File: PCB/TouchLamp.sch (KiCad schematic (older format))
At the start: 14 parts, among them IC1 ATTINY2313-P, P1 PWR_LED_ISP, P3 Sensor, Q1 BC817-40, U1 LM78L05

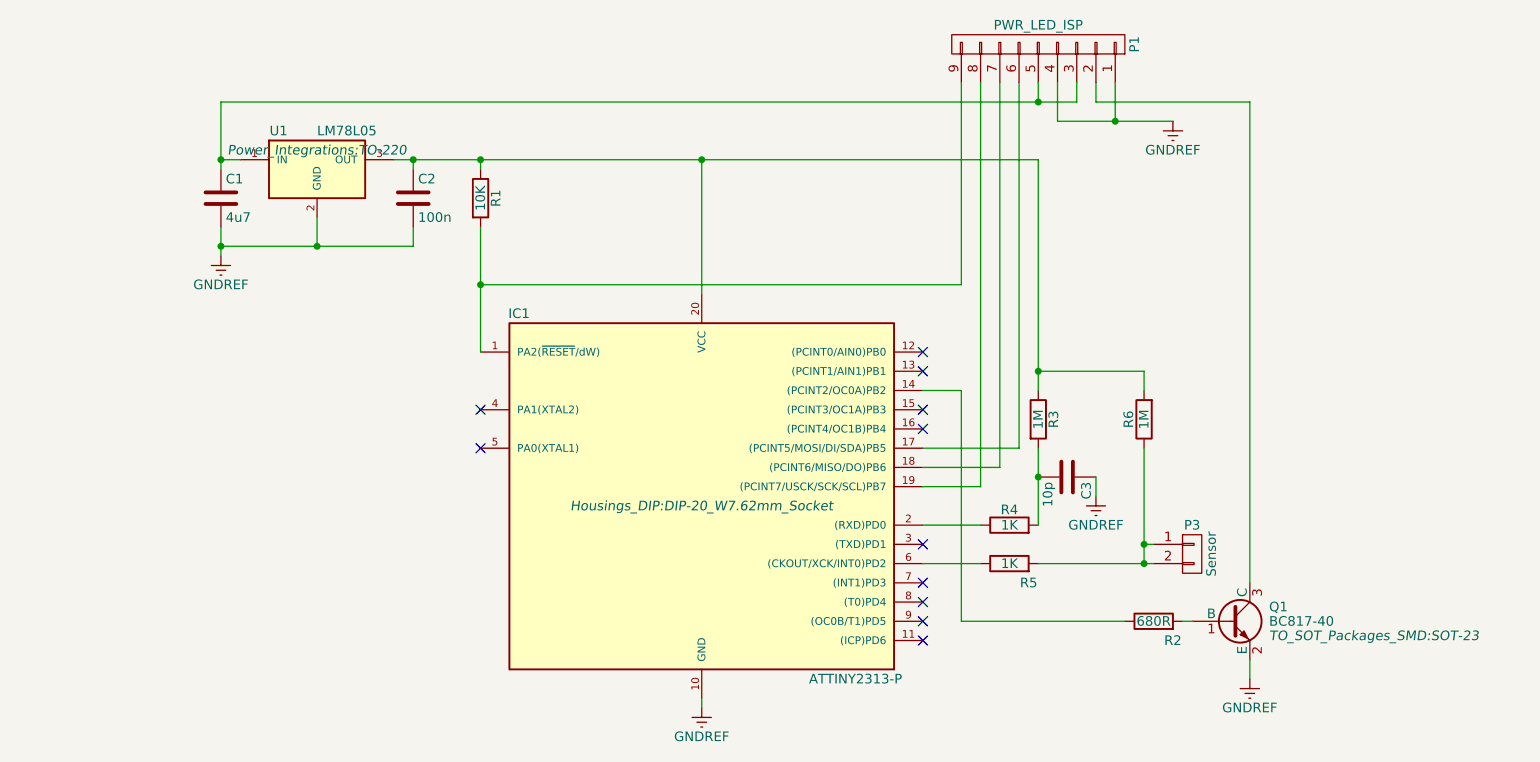
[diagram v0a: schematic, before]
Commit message: optimized the PCB and adjusted the FW
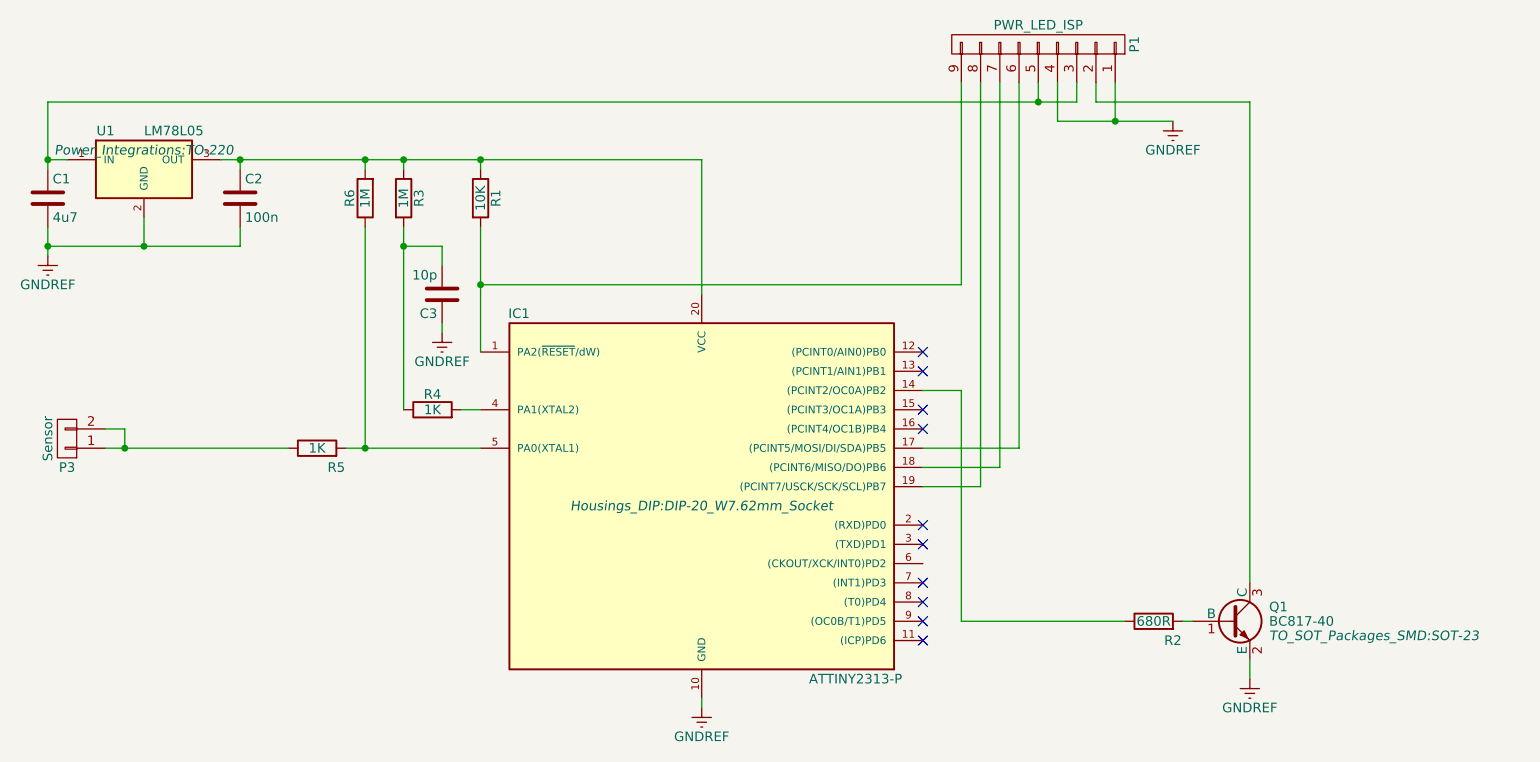
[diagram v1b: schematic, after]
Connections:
- net at IC1.2 ((RXD)PD0): no longer R4.1
- net at IC1.4 (PA1(XTAL2)): now also R4.2
- net at IC1.5 (PA0(XTAL1)): now also R5.2, R6.1
- net at IC1.6 ((CKOUT/XCK/INT0)PD2): no longer R5.1
- net at C3.2, R3.2: now also R4.1; no longer R4.2
- net at P3.1 (P1), P3.2 (P2): now also R5.1; no longer R5.2, R6.1
- no-connect marks 11 -> 10
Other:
- moved on the sheet: C1, C2, C3, P3, R3, R4, R5, R6, U1
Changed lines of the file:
@@
 L LM7805CT U1
 U 1 1 58A03CD1
-P 4550 1950
-F 0 "U1" H 4350 2150 50  0000 C CNN
-F 1 "LM78L05" H 4550 2150 50  0000 L CNN
-F 2 "Power_Integrations:TO-220" H 4550 2050 50  0000 C CIN
-F 3 "" H 4550 1950 50  0000 C CNN
-	1    4550 1950
+P 3650 1950
+F 0 "U1" H 3450 2150 50  0000 C CNN
+F 1 "LM78L05" H 3650 2150 50  0000 L CNN
+F 2 "Power_Integrations:TO-220" H 3650 2050 50  0000 C CIN
+F 3 "" H 3650 1950 50  0000 C CNN
+	1    3650 1950
 	1    0    0    -1
 $EndComp
@@
 L C C2
 U 1 1 58A03D67
-P 5050 2100
-F 0 "C2" H 5075 2200 50  0000 L CNN
-F 1 "100n" H 5075 2000 50  0000 L CNN
-F 2 "Capacitors_SMD:C_0805_HandSoldering" H 5088 1950 50  0001 C CNN
-F 3 "" H 5050 2100 50  0000 C CNN
-	1    5050 2100
+P 4150 2100
+F 0 "C2" H 4175 2200 50  0000 L CNN
+F 1 "100n" H 4175 2000 50  0000 L CNN
+F 2 "Capacitors_SMD:C_0805_HandSoldering" H 4188 1950 50  0001 C CNN
+F 3 "" H 4150 2100 50  0000 C CNN
+	1    4150 2100
 	1    0    0    -1
 $EndComp
@@
 L C C3
 U 1 1 58A03E2E
-P 8450 3550
-F 0 "C3" H 8475 3650 50  0000 L CNN
-F 1 "10p" H 8475 3450 50  0000 L CNN
-F 2 "Capacitors_SMD:C_0805_HandSoldering" H 8488 3400 50  0001 C CNN
-F 3 "" H 8450 3550 50  0000 C CNN
-	1    8450 3550
-	0    1    1    0
+P 5200 2600
+F 0 "C3" H 5225 2700 50  0000 L CNN
+F 1 "10p" H 5225 2500 50  0000 L CNN
+F 2 "Capacitors_SMD:C_0805_HandSoldering" H 5238 2450 50  0001 C CNN
+F 3 "" H 5200 2600 50  0000 C CNN
+	1    5200 2600
+	-1   0    0    1
 $EndComp
 $Comp
 L GNDREF #PWR01
 U 1 1 58A04281
-P 4050 2400
-F 0 "#PWR01" H 4050 2150 50  0001 C CNN
-F 1 "GNDREF" H 4050 2250 50  0000 C CNN
-F 2 "" H 4050 2400 50  0000 C CNN
-F 3 "" H 4050 2400 50  0000 C CNN
-	1    4050 2400
+P 3150 2400
+F 0 "#PWR01" H 3150 2150 50  0001 C CNN
+F 1 "GNDREF" H 3150 2250 50  0000 C CNN
+F 2 "" H 3150 2400 50  0000 C CNN
+F 3 "" H 3150 2400 50  0000 C CNN
+	1    3150 2400
 	1    0    0    -1
 $EndComp
@@
 L R R3
 U 1 1 58A0449D
-P 8300 3250
-F 0 "R3" V 8380 3250 50  0000 C CNN
-F 1 "1M" V 8300 3250 50  0000 C CNN
-F 2 "Resistors_SMD:R_0805_HandSoldering" V 8230 3250 50  0001 C CNN
-F 3 "" H 8300 3250 50  0000 C CNN
-	1    8300 3250
+P 5000 2100
+F 0 "R3" V 5080 2100 50  0000 C CNN
+F 1 "1M" V 5000 2100 50  0000 C CNN
+F 2 "Resistors_SMD:R_0805_HandSoldering" V 4930 2100 50  0001 C CNN
+F 3 "" H 5000 2100 50  0000 C CNN
+	1    5000 2100
 	1    0    0    -1
 $EndComp
@@
 L R R6
 U 1 1 58A044FF
-P 8850 3250
-F 0 "R6" V 8930 3250 50  0000 C CNN
-F 1 "1M" V 8850 3250 50  0000 C CNN
-F 2 "Resistors_SMD:R_0805_HandSoldering" V 8780 3250 50  0001 C CNN
-F 3 "" H 8850 3250 50  0000 C CNN
-	1    8850 3250
+P 4800 2100
+F 0 "R6" V 4880 2100 50  0000 C CNN
+F 1 "1M" V 4800 2100 50  0000 C CNN
+F 2 "Resistors_SMD:R_0805_HandSoldering" V 4730 2100 50  0001 C CNN
+F 3 "" H 4800 2100 50  0000 C CNN
+	1    4800 2100
 	-1   0    0    1
 $EndComp
@@
 L GNDREF #PWR03
 U 1 1 58A04606
-P 8600 3650
-F 0 "#PWR03" H 8600 3400 50  0001 C CNN
-F 1 "GNDREF" H 8600 3500 50  0000 C CNN
-F 2 "" H 8600 3650 50  0000 C CNN
-F 3 "" H 8600 3650 50  0000 C CNN
-	1    8600 3650
+P 5200 2800
+F 0 "#PWR03" H 5200 2550 50  0001 C CNN
+F 1 "GNDREF" H 5200 2650 50  0000 C CNN
+F 2 "" H 5200 2800 50  0000 C CNN
+F 3 "" H 5200 2800 50  0000 C CNN
+	1    5200 2800
 	1    0    0    -1
 $EndComp
@@
 L R R4
 U 1 1 58A04952
-P 8150 3800
-F 0 "R4" V 8230 3800 50  0000 C CNN
-F 1 "1K" V 8150 3800 50  0000 C CNN
-F 2 "Resistors_SMD:R_0805_HandSoldering" V 8080 3800 50  0001 C CNN
-F 3 "" H 8150 3800 50  0000 C CNN
-	1    8150 3800
+P 5150 3200
+F 0 "R4" V 5230 3200 50  0000 C CNN
+F 1 "1K" V 5150 3200 50  0000 C CNN
+F 2 "Resistors_SMD:R_0805_HandSoldering" V 5080 3200 50  0001 C CNN
+F 3 "" H 5150 3200 50  0000 C CNN
+	1    5150 3200
 	0    -1   -1   0
 $EndComp
@@
 L R R5
 U 1 1 58A04A05
-P 8150 4000
-F 0 "R5" V 8050 3900 50  0000 C CNN
-F 1 "1K" V 8150 4000 50  0000 C CNN
-F 2 "Resistors_SMD:R_0805_HandSoldering" V 8080 4000 50  0001 C CNN
-F 3 "" H 8150 4000 50  0000 C CNN
-	1    8150 4000
+P 4550 3400
+F 0 "R5" V 4450 3300 50  0000 C CNN
+F 1 "1K" V 4550 3400 50  0000 C CNN
+F 2 "Resistors_SMD:R_0805_HandSoldering" V 4480 3400 50  0001 C CNN
+F 3 "" H 4550 3400 50  0000 C CNN
+	1    4550 3400
 	0    -1   -1   0
 $EndComp
@@
 	1    0    0    -1
 $EndComp
-NoConn ~ 5400 3200
-NoConn ~ 5400 3400
+NoConn ~ 7700 3800
 NoConn ~ 7700 3300
 NoConn ~ 7700 3200
@@
 L C C1
 U 1 1 58A95423
-P 4050 2100
-F 0 "C1" H 4075 2200 50  0000 L CNN
-F 1 "4u7" H 4075 2000 50  0000 L CNN
-F 2 "Capacitors_SMD:C_0805_HandSoldering" H 4088 1950 50  0001 C CNN
-F 3 "" H 4050 2100 50  0000 C CNN
-	1    4050 2100
+P 3150 2100
+F 0 "C1" H 3175 2200 50  0000 L CNN
+F 1 "4u7" H 3175 2000 50  0000 L CNN
+F 2 "Capacitors_SMD:C_0805_HandSoldering" H 3188 1950 50  0001 C CNN
+F 3 "" H 3150 2100 50  0000 C CNN
+	1    3150 2100
 	1    0    0    -1
 $EndComp
@@
 L CONN_01X02 P3
 U 1 1 58A9580F
-P 9100 3950
-F 0 "P3" H 9100 4100 50  0000 C CNN
-F 1 "Sensor" V 9200 3950 50  0000 C CNN
-F 2 "Socket_Strips:Socket_Strip_Angled_1x02_Pitch2.54mm" H 9100 3950 50  0001 C CNN
-F 3 "" H 9100 3950 50  0000 C CNN
-	1    9100 3950
-	1    0    0    -1
-$EndComp
-Wire Wire Line
-	4050 2250 4050 2400
-Wire Wire Line
-	4550 2350 4550 2200
-Connection ~ 4550 2350
-Wire Wire Line
-	6550 1900 6550 2600
-Connection ~ 4050 1900
-Connection ~ 4050 2350
-Wire Wire Line
-	6550 4750 6550 4700
-Wire Wire Line
-	9400 4600 9400 4500
-Wire Wire Line
-	5050 2350 5050 2250
-Wire Wire Line
-	5050 1950 5050 1900
-Connection ~ 5050 1900
-Wire Wire Line
-	5400 1950 5400 1900
-Connection ~ 5400 1900
-Wire Wire Line
-	5400 2250 5400 2900
-Wire Wire Line
-	8200 1500 8200 3400
-Wire Wire Line
-	8200 3400 7700 3400
-Wire Wire Line
-	8100 1500 8100 3500
-Wire Wire Line
-	8100 3500 7700 3500
-Wire Wire Line
-	8000 1500 8000 3600
-Wire Wire Line
-	8000 3600 7700 3600
-Wire Wire Line
-	9050 4300 9100 4300
-Wire Wire Line
-	4050 1600 4050 1950
-Wire Wire Line
-	4050 1900 4150 1900
-Wire Wire Line
-	4050 1600 8500 1600
-Wire Wire Line
-	8300 1600 8300 1500
-Connection ~ 8300 1600
-Wire Wire Line
-	4050 2350 5050 2350
-Wire Wire Line
-	7900 1500 7900 2550
-Wire Wire Line
-	9400 1600 9400 4100
+P 3250 3350
+F 0 "P3" H 3250 3500 50  0000 C CNN
+F 1 "Sensor" V 3350 3350 50  0000 C CNN
+F 2 "Socket_Strips:Socket_Strip_Angled_1x02_Pitch2.54mm" H 3250 3350 50  0001 C CNN
+F 3 "" H 3250 3350 50  0000 C CNN
+	1    3250 3350
+	-1   0    0    1
+$EndComp
 $Comp
 L CONN_01X09 P1
@@
 	0    1    -1   0
 $EndComp
-Wire Wire Line
-	8500 1600 8500 1500
-Wire Wire Line
-	8400 1500 8400 1700
-Wire Wire Line
-	8400 1700 9000 1700
 NoConn ~ 7700 4300
 NoConn ~ 7700 3000
 NoConn ~ 7700 2900
 NoConn ~ 7700 4400
-Wire Wire Line
-	8600 1600 9400 1600
 NoConn ~ 7700 4100
 NoConn ~ 7700 4200
 NoConn ~ 7700 3900
 Wire Wire Line
+	3150 2250 3150 2400
+Wire Wire Line
+	3650 2350 3650 2200
+Connection ~ 3650 2350
+Wire Wire Line
+	6550 1900 6550 2600
+Connection ~ 3150 1900
+Connection ~ 3150 2350
+Wire Wire Line
+	6550 4750 6550 4700
+Wire Wire Line
+	9400 4600 9400 4500
+Wire Wire Line
+	4150 2350 4150 2250
+Wire Wire Line
+	4150 1950 4150 1900
+Connection ~ 4150 1900
+Wire Wire Line
+	5400 1950 5400 1900
+Connection ~ 5400 1900
+Wire Wire Line
+	5400 2250 5400 2900
+Wire Wire Line
+	8200 1500 8200 3400
+Wire Wire Line
+	8200 3400 7700 3400
+Wire Wire Line
+	8100 1500 8100 3500
+Wire Wire Line
+	8100 3500 7700 3500
+Wire Wire Line
+	8000 1500 8000 3600
+Wire Wire Line
+	8000 3600 7700 3600
+Wire Wire Line
+	9050 4300 9100 4300
+Wire Wire Line
+	3150 1600 3150 1950
+Wire Wire Line
+	3150 1900 3250 1900
+Wire Wire Line
+	3150 1600 8500 1600
+Wire Wire Line
+	8300 1600 8300 1500
+Connection ~ 8300 1600
+Wire Wire Line
+	3150 2350 4150 2350
+Wire Wire Line
+	7900 1500 7900 2550
+Wire Wire Line
+	9400 1600 9400 4100
+Wire Wire Line
+	8500 1600 8500 1500
+Wire Wire Line
+	8400 1500 8400 1700
+Wire Wire Line
+	8400 1700 9000 1700
+Wire Wire Line
+	8600 1600 9400 1600
+Wire Wire Line
 	8600 1600 8600 1500
 Wire Wire Line
@@
 Connection ~ 8700 1700
 Wire Wire Line
-	7700 4000 8000 4000
-Wire Wire Line
-	8850 3400 8850 4000
-Wire Wire Line
-	8850 3900 8900 3900
-Connection ~ 8850 4000
-Wire Wire Line
-	7700 3800 8000 3800
-Wire Wire Line
-	8600 3650 8600 3550
-Wire Wire Line
-	8300 3400 8300 3800
-Connection ~ 8850 3900
-Connection ~ 8300 3550
-Wire Wire Line
-	8300 1900 8300 3100
-Wire Wire Line
-	8300 3000 8850 3000
-Wire Wire Line
-	8850 3000 8850 3100
-Wire Wire Line
-	4950 1900 8300 1900
-Connection ~ 8300 3000
-Connection ~ 6550 1900
-Wire Wire Line
 	7900 2550 5400 2550
 Connection ~ 5400 2550
 Wire Wire Line
-	8300 4000 8900 4000
-Wire Wire Line
 	7700 3100 7900 3100
 Wire Wire Line
@@
 Wire Wire Line
 	7900 4300 8750 4300
+Wire Wire Line
+	5300 3200 5400 3200
+Wire Wire Line
+	5000 2250 5000 3200
+Wire Wire Line
+	5000 1950 5000 1900
+Connection ~ 5000 1900
+Wire Wire Line
+	5200 2450 5200 2350
+Wire Wire Line
+	5200 2350 5000 2350
+Connection ~ 5000 2350
+Wire Wire Line
+	5200 2800 5200 2750
+Wire Wire Line
+	4700 3400 5400 3400
+Wire Wire Line
+	4800 1950 4800 1900
+Connection ~ 4800 1900
+Wire Wire Line
+	4800 2250 4800 3400
+Wire Wire Line
+	4050 1900 6550 1900
+Wire Wire Line
+	3450 3300 3550 3300
+Wire Wire Line
+	3550 3300 3550 3400
+Wire Wire Line
+	3450 3400 4400 3400
+Connection ~ 3550 3400
+Connection ~ 4800 3400
 $EndSCHEMATC
